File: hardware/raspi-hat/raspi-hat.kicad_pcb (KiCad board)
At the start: 4 copper layers, 65 x 57 mm, 58 parts, among them J1 Conn_02x05_Counter_Clockwise, J2 Conn_01x03_Pin, J3 ATX-20, J4 Raspberry_Pi_4, J5 USB3_A, Q1 FDMS86101, Q2 FDMS86101, Q3 FDMS86101, Q4 FDMS86101, Q5 FDMS86101, Q7 FDMS86101, U1 STSPIN32G4, Y1 Crystal_GND23_Small

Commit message: - updated pinout - updated cube mx
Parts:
- moved C5 0.62 mm to (145.3, 135.2)
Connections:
- net /controller/shunt-amp/OP+ renamed /controller/shunt1_op+
- net /controller/shunt-amp/OP- renamed /controller/shunt1_op-
- net /controller/shunt-amp1/OP+ renamed /controller/shunt2_op+
- net /controller/shunt-amp2/OP+ renamed /controller/shunt3_op+
- net /controller/shunt-amp2/OP- renamed /controller/shunt3_op-
- net Net-(U1-PA0) renamed /controller/v_bus_meas
- R11 pad 2: /controller/shunt-amp1/OP- -> /controller/shunt2_op-
- R14 pad 1: /controller/shunt-amp1/OP- -> /controller/shunt2_op-
- R14 pad 2: /controller/shunt-amp1/OPOUT -> /controller/shunt2_opout
- R19 pad 2: /controller/shunt-amp2/OPOUT -> /controller/shunt3_opout
- R9 pad 2: /controller/shunt-amp/OPOUT -> /controller/shunt1_opout
- U1 pad 12: unconnected-(U1-PC3-Pad12) -> /controller/ntc
- U1 pad 15: /controller/shunt-amp/OPOUT -> /controller/shunt1_opout
- U1 pad 17: /controller/ntc -> /controller/shunt1_opout
- U1 pad 18: unconnected-(U1-PA5-Pad18) -> /controller/shunt2_op-
- U1 pad 19: /controller/shunt-amp1/OPOUT -> /controller/shunt2_opout
- U1 pad 21: unconnected-(U1-PC4-Pad21) -> /controller/shunt2_opout
- U1 pad 22: /controller/shunt-amp1/OP- -> /controller/shunt3_opout
- U1 pad 24: /controller/shunt-amp2/OPOUT -> /controller/shunt3_opout
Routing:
- net /controller/ntc: track 48.3 -> 74.0 mm, vias 4 -> 6
- net /controller/shunt2_opout: track 0.00 -> 20.7 mm, vias 0 -> 4
- net /controller/shunt2_op-: track 0.00 -> 18.6 mm, vias 0 -> 3
- net /controller/shunt3_opout: track 0.00 -> 16.0 mm, vias 0 -> 3
- net /controller/shunt-amp1/OP-: track 13.1 -> 0.00 mm, vias 2 -> 0
- net /controller/shunt-amp1/OPOUT: track 12.9 -> 0.00 mm, vias 3 -> 0
- net /controller/shunt-amp2/OPOUT: track 11.4 -> 0.00 mm, vias 2 -> 0
- net /controller/shunt-amp/OPOUT: track 7.88 -> 0.00 mm
- net /controller/shunt1_opout: track 0.00 -> 7.46 mm
- net /controller/shunt1_op-: track 8.93 -> 12.9 mm, vias 0 -> 3
- net /controller/inverter/HS1: track 33.5 -> 34.5 mm
- net /controller/phase_u: track 26.2 -> 25.5 mm
- net /controller/inverter/LS1: track 37.7 -> 38.3 mm
- net /GND: vias 119 -> 118

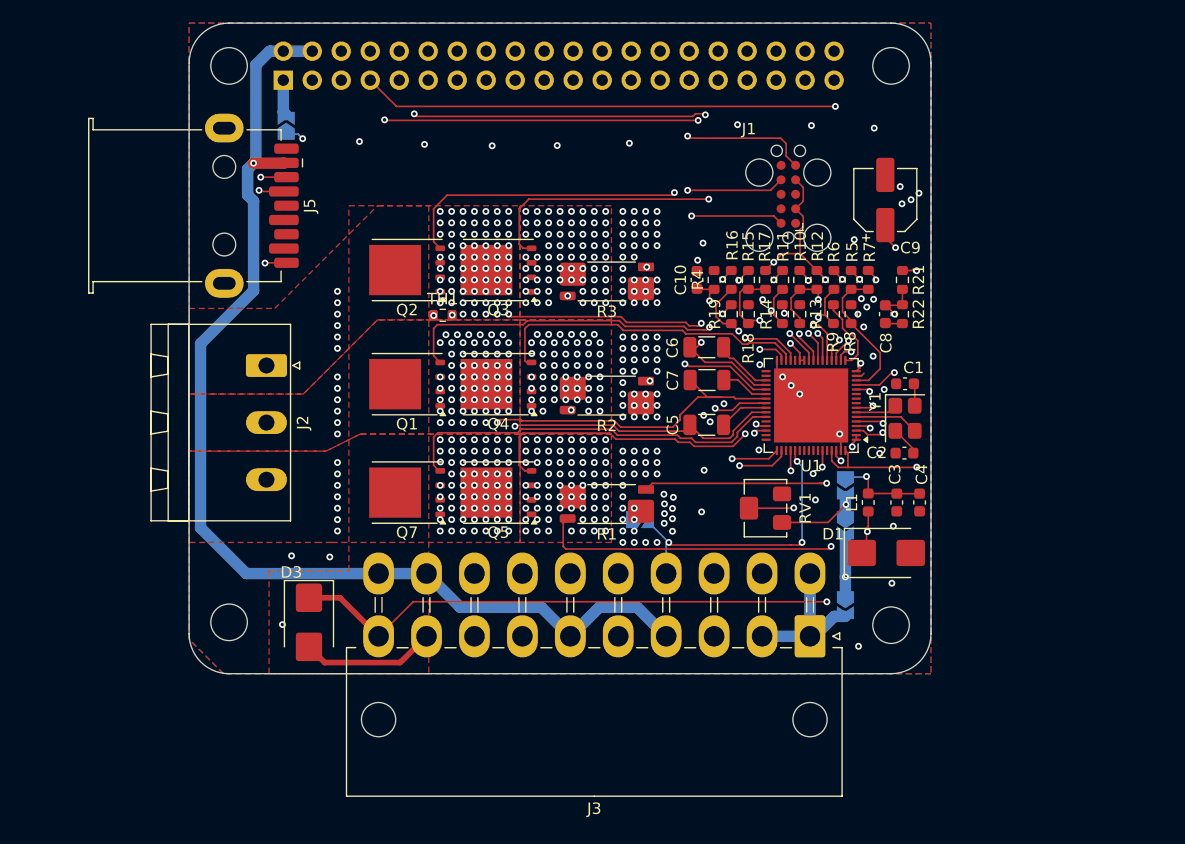
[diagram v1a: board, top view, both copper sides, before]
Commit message: - added some more parts for temperature measurement - added capacitor
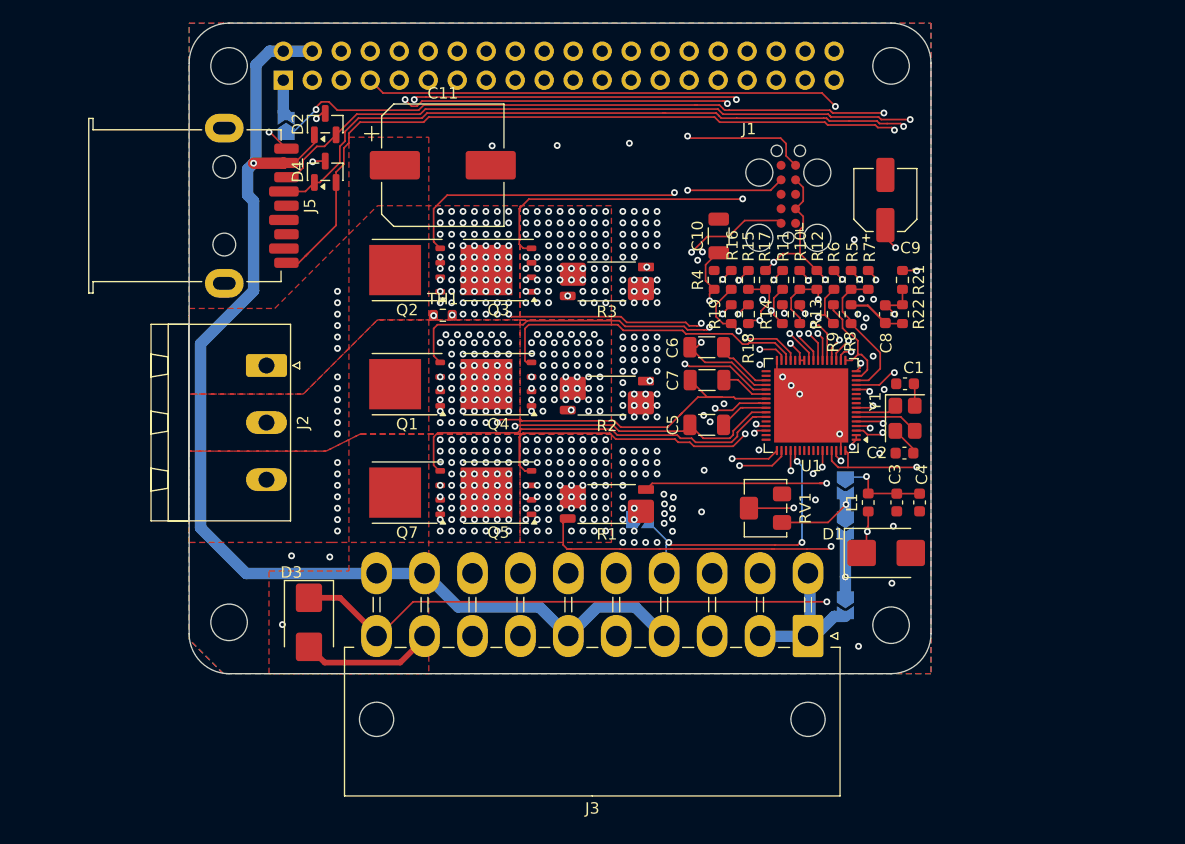
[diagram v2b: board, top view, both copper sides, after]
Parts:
- added C11: 220u, Capacitor_SMD:CP_Elec_10x14.3, F.Cu at (122.2, 112.5)
- added D2: SP0502BAHT, Package_TO_SOT_SMD:SOT-23, F.Cu at (111.9, 108.8)
- added D4: SP0502BAHT, Package_TO_SOT_SMD:SOT-23, F.Cu at (111.9, 113.0)
- C10: footprint Capacitor_SMD:C_0603_1608Metric -> Capacitor_SMD:C_1206_3216Metric
- C8: value 100n -> 1u
- C9: value 25u -> 47u
- moved C10 4.29 mm to (146.4, 118.7)
- moved J3 0.18 mm to (154.2, 153.7)
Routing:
- net /GND: track 11.7 -> 21.8 mm
- net /controller/hall_2: track 83.7 -> 92.3 mm, vias 3 -> 2
- net /controller/hall_1: track 85.3 -> 91.2 mm, vias 3 -> 2
- net /+3V3: track 98.5 -> 103.9 mm
- net /+5V: track 98.0 -> 102.1 mm
- net /controller/hall_3: track 84.9 -> 87.9 mm, vias 3 -> 2
- net /controller/inverter/LS3: track 38.9 -> 41.4 mm
- net /controller/ntc: track 74.0 -> 76.5 mm
- net /controller/shunt1_opout: track 7.46 -> 9.76 mm
- net /controller/uart_tx: track 62.1 -> 64.0 mm
- net /controller/reset: track 59.8 -> 61.4 mm
- net /controller/uart_rx: track 64.8 -> 66.1 mm
- net /controller/shunt2_opout: track 20.7 -> 19.3 mm
- net /controller/shunt3_op+: track 14.0 -> 13.3 mm

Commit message: replaced usb connector for hall sensors with usbc
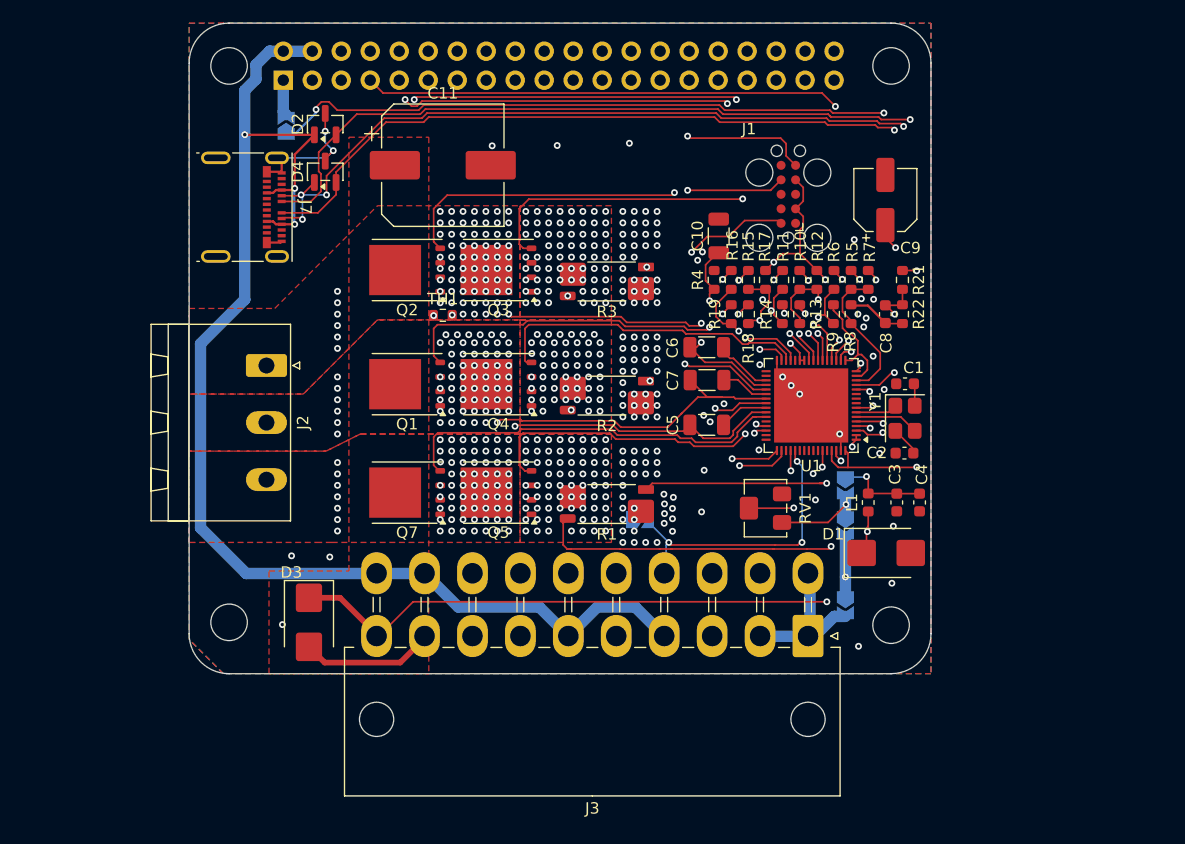
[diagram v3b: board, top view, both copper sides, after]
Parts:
- removed J5: USB3_A, Connector_USB:USB3_A_Receptacle_Wuerth_692122030100
- added J7: USB_C_Receptacle, Connector_USB:USB_C_Receptacle_Molex_105450-0101, F.Cu at (104.9, 116.1)
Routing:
- net /+5V: track 102.1 -> 114.7 mm, vias 1 -> 3
- net /GND: track 21.8 -> 31.7 mm, vias 118 -> 117
- net /controller/hall_2: track 92.3 -> 87.6 mm
- net /controller/hall_1: track 91.2 -> 95.4 mm, vias 2 -> 5
- net /controller/hall_3: track 87.9 -> 91.1 mm
- net /controller/shunt2_opout: track 19.3 -> 17.8 mm
- net /+3V3: track 103.9 -> 103.0 mm
- net /controller/inverter/LS3: track 41.4 -> 40.9 mm

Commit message: fixed bom
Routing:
- net /controller/hall_2: track 87.6 -> 89.0 mm
- net /controller/hall_1: track 95.4 -> 96.8 mm
- net /controller/boot: track 75.2 -> 75.8 mm
- net /controller/phase_u: vias 70 -> 69
- net /GND: vias 117 -> 258
- net /+12V: vias 3 -> 75
- added copper zone on B.Cu, net /+12V

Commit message: updated hardware
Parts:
- added C12: 1u, Capacitor_SMD:C_0603_1608Metric, F.Cu at (86.0, 154.5)
- added C13: 1u, Capacitor_SMD:C_0603_1608Metric, F.Cu at (158.0, 140.0)
- added C14: 1u, Capacitor_SMD:C_0603_1608Metric, F.Cu at (95.5, 151.5)
- added C15: 1u, Capacitor_SMD:C_0603_1608Metric, F.Cu at (107.0, 146.0)
- added C16: 1u, Capacitor_SMD:C_0603_1608Metric, F.Cu at (107.0, 147.5)
- added C17: 1u, Capacitor_SMD:C_0603_1608Metric, F.Cu at (107.0, 149.0)
- added C18: 1u, Capacitor_SMD:C_0603_1608Metric, F.Cu at (89.0, 137.5)
- added C19: 1u, Capacitor_SMD:C_0603_1608Metric, F.Cu at (89.0, 140.0)
- added C20: 1u, Capacitor_SMD:C_0603_1608Metric, F.Cu at (89.0, 142.5)
- added C21: 1u, Capacitor_SMD:C_0603_1608Metric, F.Cu at (175.5, 126.3)
- added C22: 1u, Capacitor_SMD:C_0603_1608Metric, F.Cu at (175.5, 128.8)
- added C23: 1u, Capacitor_SMD:C_0603_1608Metric, F.Cu at (175.5, 131.3)
- added C24: 1u, Capacitor_SMD:C_0603_1608Metric, F.Cu at (179.5, 118.8)
- added C25: 1u, Capacitor_SMD:C_0603_1608Metric, F.Cu at (179.5, 121.3)
- added C26: 1u, Capacitor_SMD:C_0603_1608Metric, F.Cu at (179.5, 123.8)
- added C27: 1u, Capacitor_SMD:C_0603_1608Metric, F.Cu at (179.5, 126.3)
- added C28: 1u, Capacitor_SMD:C_0603_1608Metric, F.Cu at (179.5, 128.8)
- added C29: 1u, Capacitor_SMD:C_0603_1608Metric, F.Cu at (179.5, 131.3)
- added C30: 1u, Capacitor_SMD:C_0603_1608Metric, F.Cu at (183.5, 118.8)
- added C31: 1u, Capacitor_SMD:C_0603_1608Metric, F.Cu at (183.5, 121.3)
- added C32: 1u, Capacitor_SMD:C_0603_1608Metric, F.Cu at (183.5, 123.8)

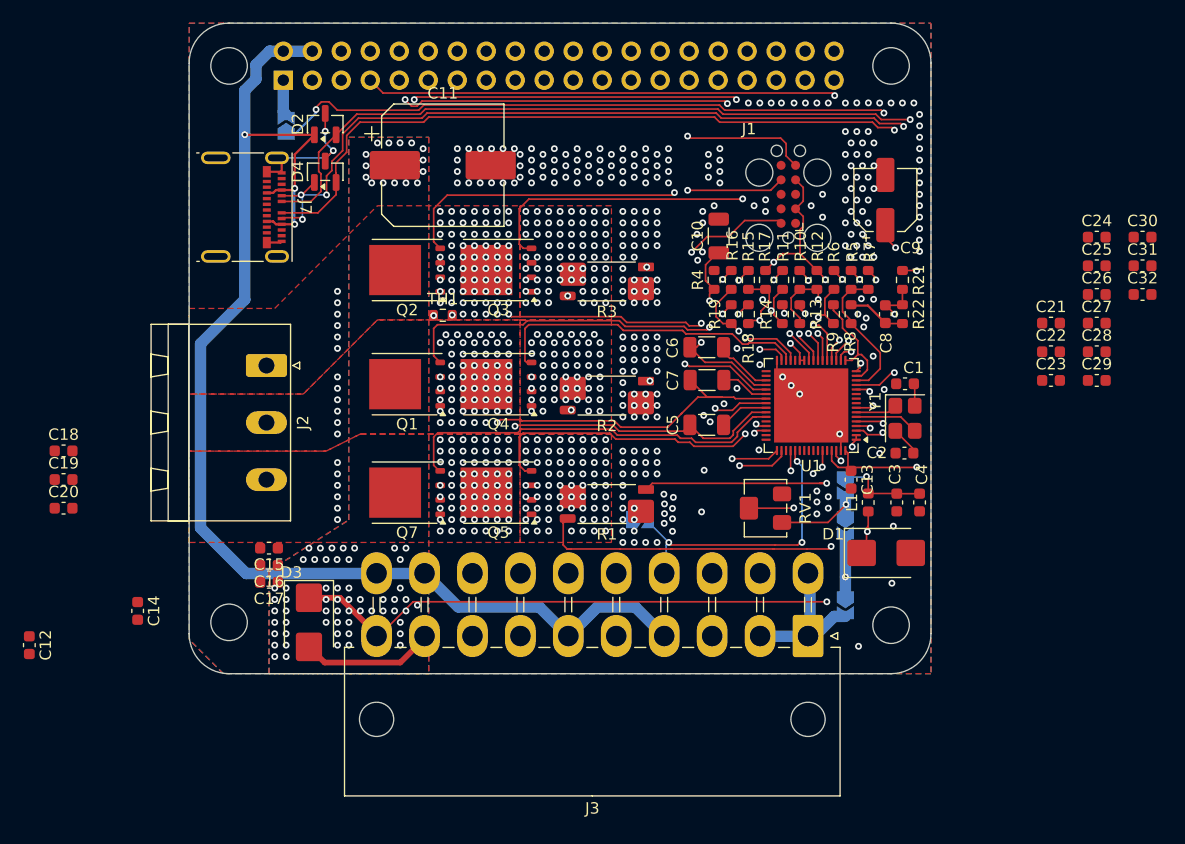
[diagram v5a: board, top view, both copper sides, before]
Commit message: removed capacitors that i couln't fit
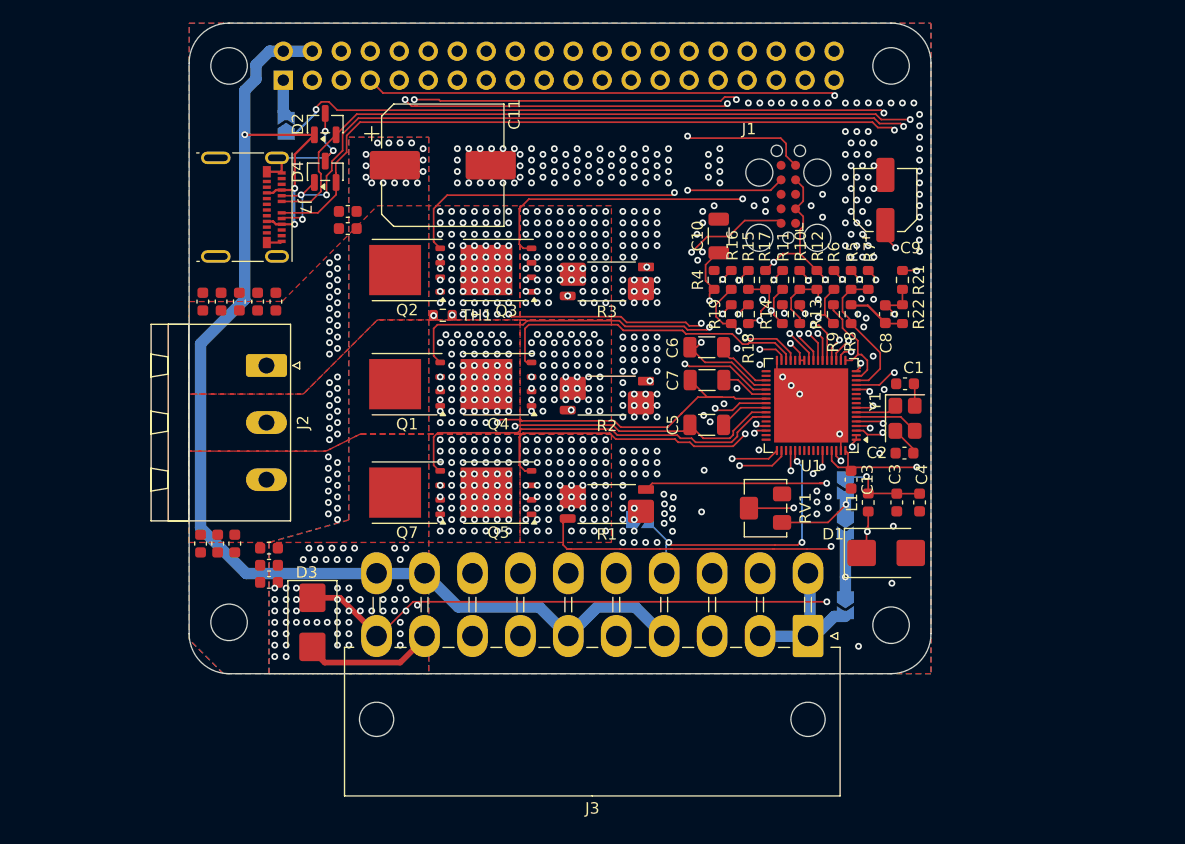
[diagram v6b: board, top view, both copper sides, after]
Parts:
- removed C21, C22, C28, C29, C30, C31, C32: 1u, Capacitor_SMD:C_0603_1608Metric
- moved C27 76.7 mm to (102.8, 124.4), turned to 90 degrees
- moved C26 75.1 mm to (104.4, 124.4), turned to 90 degrees
- moved C23 74.6 mm to (101.2, 124.4), turned to 90 degrees
- moved C25 73.6 mm to (106.0, 124.4), turned to 90 degrees
- moved C24 72.1 mm to (107.6, 124.4), turned to 90 degrees
- moved C12 47.1 mm to (113.9, 116.5), turned to 180 degrees
- moved C14 38.2 mm to (113.9, 118.0), turned to 180 degrees
- moved C18 17.1 mm to (104.0, 145.6), turned to -90 degrees
- moved C19 14.6 mm to (102.5, 145.6), turned to -90 degrees
- moved C20 12.4 mm to (101.0, 145.6), turned to -90 degrees
- moved D3 0.30 mm to (110.8, 152.5)
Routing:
- net /controller/phase_w: vias 75 -> 87
- net /controller/phase_v: vias 65 -> 71
- net /controller/phase_u: vias 69 -> 75
- net /+12V: vias 75 -> 78
